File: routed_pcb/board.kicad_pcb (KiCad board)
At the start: 2 copper layers, 100 x 100 mm, 29 parts

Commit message: board cleanup
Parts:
- ?: footprint Button_Switch_SMD:SW_SPST_B3U-1000P -> Library:SW_SPST_B3U-1000P
- B1: footprint kbd:ResetSW -> Library:ResetSW
- MCU1: footprint ProMicro -> Library:ProMicro
- S1, S10, S11, S12, S13, S14, S15, S16, S17, S2, S3, S4, S5, S6, S7, S8, S9: footprint key-switches -> Library:key-switches
- T1: footprint E73:SPDT_C128955 -> Library:SPDT_C128955
- TRRS1: footprint TRRS-PJ-320A-dual -> Library:TRRS-PJ-320A-dual
- _2: footprint JST_PH_S2B-PH-K_02x2.00mm_Angled -> Library:JST_PH_S2B-PH-K_02x2.00mm_Angled
- _3, _4, _5, _6, _7, _8: footprint MountingHole_2.2mm_M2_Pad_Via -> Library:MountingHole_2.2mm_M2_Pad_Via
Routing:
- net VCC: track 210.7 -> 143.3 mm
- net GND: track 180.3 -> 207.1 mm
- net thumb_reachy: track 93.9 -> 81.1 mm
- net matrix_inner_top: track 144.0 -> 154.2 mm, vias 2 -> 3
- net matrix_ring_bottom: track 34.0 -> 40.6 mm
- net Switch18: track 165.7 -> 159.7 mm
- net matrix_index_home: track 70.4 -> 64.9 mm
- net matrix_pinky_bottom: track 40.0 -> 36.2 mm
- net matrix_inner_bottom: track 81.5 -> 78.5 mm
- net matrix_index_bottom: track 62.5 -> 59.5 mm
- net thumb_tucky: track 81.6 -> 79.9 mm
- net matrix_inner_home: track 114.6 -> 113.2 mm
- net RST: track 48.7 -> 47.5 mm

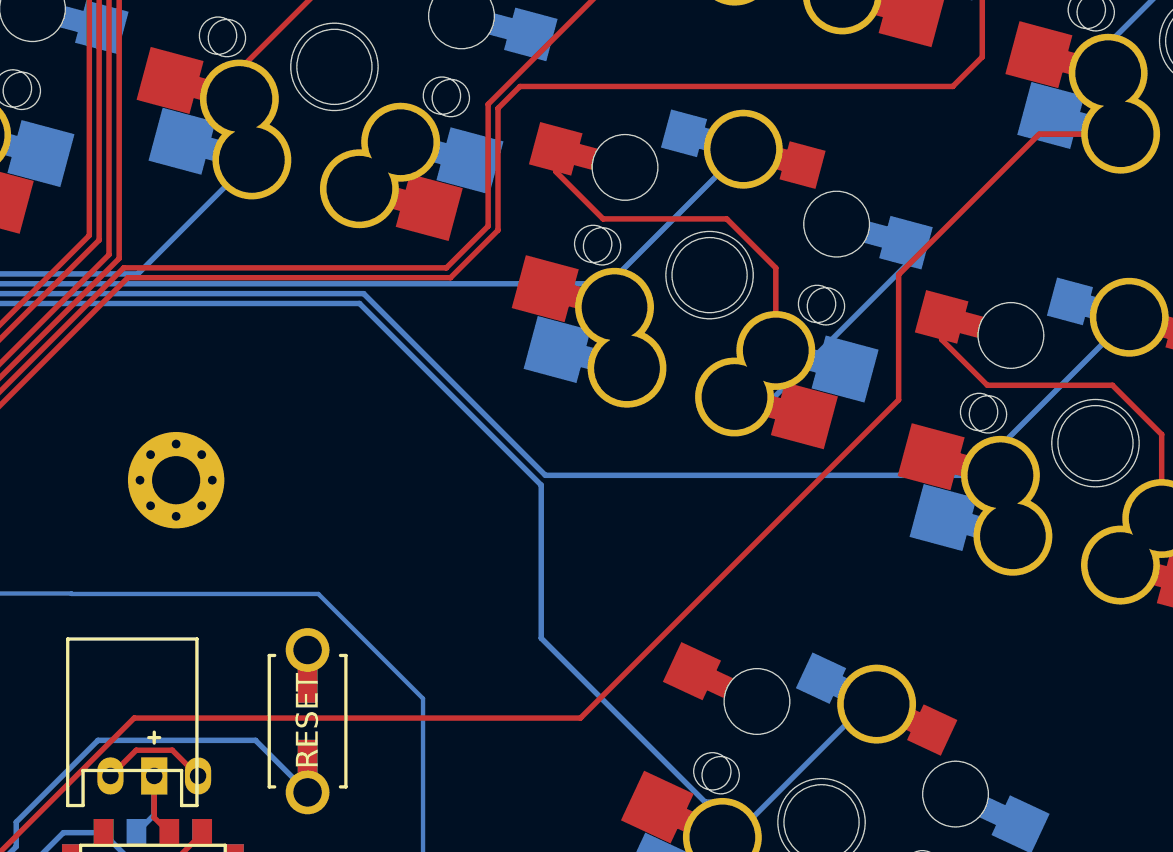
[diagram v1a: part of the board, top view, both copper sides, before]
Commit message: added plate
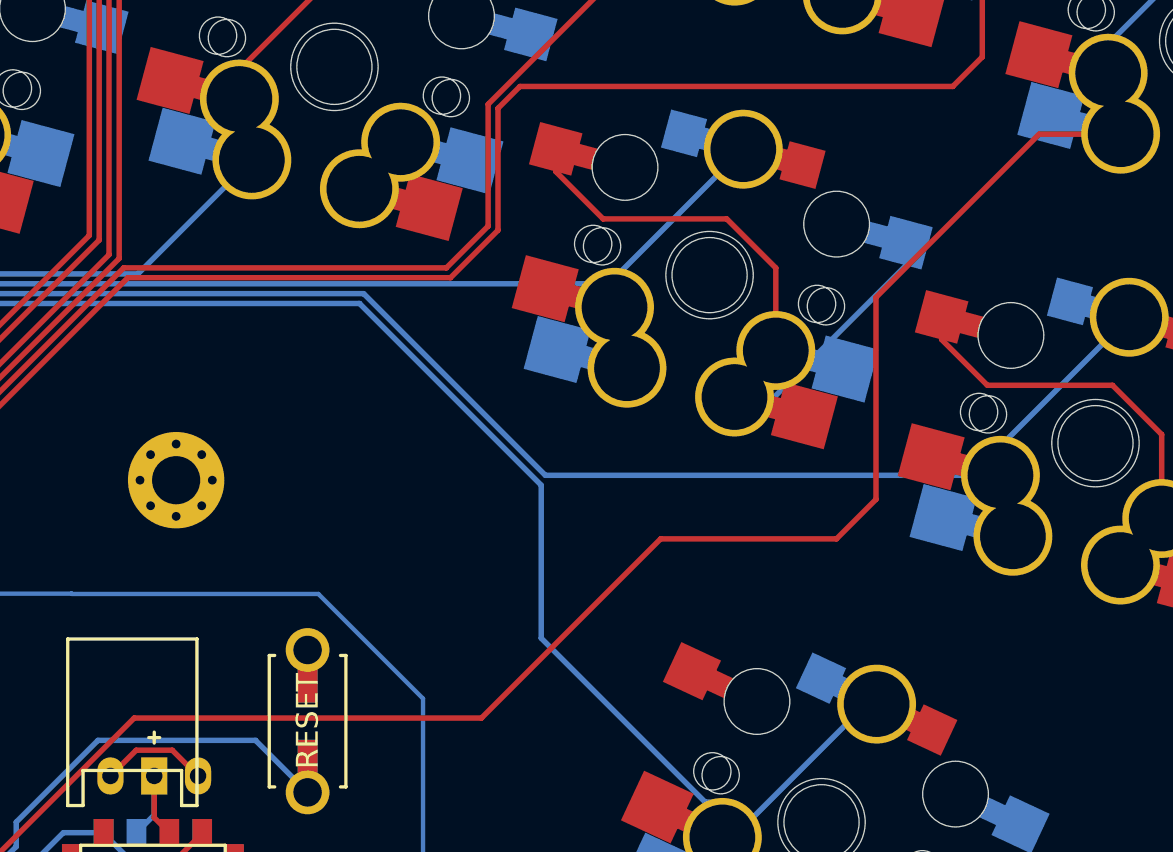
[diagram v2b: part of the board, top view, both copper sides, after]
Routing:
- net matrix_inner_home: track 113.2 -> 115.2 mm
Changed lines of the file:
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@@
       (outputformat 1)
       (mirror false)
-      (drillshape 1)
+      (drillshape 0)
       (scaleselection 1)
-      (outputdirectory "")
+      (outputdirectory "gerbers/")
     )
   )
@@
   (segment (start 146.15277 134.562217) (end 140.275219 140.439768) (width 0.25) (layer "B.Cu") (net 14))
   (segment (start 85.615 139.477518) (end 91.608318 133.4842) (width 0.25) (layer "B.Cu") (net 14))
-  (segment (start 65.005 160.382) (end 65.005 157.951) (width 0.25) (layer "F.Cu") (net 15))
-  (segment (start 135.6288 132.6206) (end 135.6288 138.3356) (width 0.25) (layer "F.Cu") (net 15))
+  (segment (start 65.9312 161.3082) (end 65.005 160.382) (width 0.25) (layer "F.Cu") (net 15))
+  (segment (start 134.5946 133.6548) (end 134.5946 142.875) (width 0.25) (layer "F.Cu") (net 15))
+  (segment (start 116.586 152.8572) (end 100.734652 152.8572) (width 0.25) (layer "F.Cu") (net 15))
   (segment (start 145.762107 126.206388) (end 142.043012 126.206388) (width 0.25) (layer "F.Cu") (net 15))
-  (segment (start 94.0054 160.401) (end 93.0982 161.3082) (width 0.25) (layer "F.Cu") (net 15))
   (segment (start 65.005 157.951) (end 63.88 156.826) (width 0.25) (layer "F.Cu") (net 15))
-  (segment (start 142.043012 126.206388) (end 135.6288 132.6206) (width 0.25) (layer "F.Cu") (net 15))
-  (segment (start 65.9312 161.3082) (end 65.005 160.382) (width 0.25) (layer "F.Cu") (net 15))
-  (segment (start 121.1072 152.8572) (end 100.734652 152.8572) (width 0.25) (layer "F.Cu") (net 15))
+  (segment (start 94.0054 160.401) (end 93.0982 161.3082) (width 0.25) (layer "F.Cu") (net 15))
+  (segment (start 100.734652 152.8572) (end 94.0054 159.586452) (width 0.25) (layer "F.Cu") (net 15))
+  (segment (start 65.005 160.382) (end 65.005 157.951) (width 0.25) (layer "F.Cu") (net 15))
   (segment (start 94.0054 159.586452) (end 94.0054 160.401) (width 0.25) (layer "F.Cu") (net 15))
+  (segment (start 132.7912 144.6784) (end 124.7648 144.6784) (width 0.25) (layer "F.Cu") (net 15))
+  (segment (start 142.043012 126.206388) (end 134.5946 133.6548) (width 0.25) (layer "F.Cu") (net 15))
   (segment (start 93.0982 161.3082) (end 65.9312 161.3082) (width 0.25) (layer "F.Cu") (net 15))
-  (segment (start 135.6288 138.3356) (end 121.1072 152.8572) (width 0.25) (layer "F.Cu") (net 15))
-  (segment (start 100.734652 152.8572) (end 94.0054 159.586452) (width 0.25) (layer "F.Cu") (net 15))
+  (segment (start 134.5946 142.875) (end 132.7912 144.6784) (width 0.25) (layer "F.Cu") (net 15))
+  (segment (start 124.7648 144.6784) (end 116.586 152.8572) (width 0.25) (layer "F.Cu") (net 15))
   (segment (start 151.070332 116.209626) (end 145.192781 122.087177) (width 0.25) (layer "B.Cu") (net 15))
   (segment (start 145.192781 122.087177) (end 145.192781 123.424236) (width 0.25) (layer "B.Cu") (net 15))

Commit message: routed new pcb
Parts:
- removed the ? at (108.7, 153.0)
- removed S1, S10, S11, S12, S13, S14, S15, S16, S17, S2, S3, S4, S5, S6, S7, S8, S9: , Library:key-switches
- removed _2: , Library:JST_PH_S2B-PH-K_02x2.00mm_Angled
- removed _3, _4, _5: , Library:MountingHole_2.2mm_M2_Pad_Via
- added ?: , Button_Switch_SMD:SW_SPST_B3U-1000P, F.Cu at (110.3, 169.0)
- added SW1: , key-switches, F.Cu at (77.0, 118.6)
- added SW10: , key-switches, F.Cu at (133.8, 125.8)
- added SW11: , key-switches, F.Cu at (137.7, 107.2)
- added SW12: , key-switches, F.Cu at (141.7, 88.6)
- added SW13: , key-switches, F.Cu at (151.8, 132.5)
- added SW14: , key-switches, F.Cu at (155.7, 114.0)
- added SW15: , key-switches, F.Cu at (159.7, 95.4)
- added SW16: , key-switches, F.Cu at (118.3, 143.9)
- added SW17: , key-switches, F.Cu at (138.2, 150.7)
- added SW18: , key-switches, F.Cu at (157.8, 160.6)
- added SW2: , key-switches, F.Cu at (81.0, 100.0)
- added SW3: , key-switches, F.Cu at (84.9, 81.4)
- added SW4: , key-switches, F.Cu at (96.6, 117.9)
- added SW5: , key-switches, F.Cu at (100.5, 99.3)
- added SW6: , key-switches, F.Cu at (104.5, 80.7)
- added SW7: , key-switches, F.Cu at (116.2, 117.2)
- added SW8: , key-switches, F.Cu at (120.1, 98.6)
- added SW9: , key-switches, F.Cu at (124.1, 80.0)
- added T2: , E73:SPDT_C128955, F.Cu at (108.3, 161.0)
- added _10: , MountingHole_2.2mm_M2_Pad_Via, F.Cu at (131.3, 168.0)
- added _11: , MountingHole_2.2mm_M2_Pad_Via, F.Cu at (103.3, 135.0)
- added _12: , MountingHole_2.2mm_M2_Pad_Via, F.Cu at (71.3, 168.0)
- added _9: , MountingHole_2.2mm_M2_Pad_Via, F.Cu at (165.3, 140.0)
- B1: footprint Library:ResetSW -> kbd:ResetSW
- MCU1: footprint Library:ProMicro -> ProMicro
- T1: footprint Library:SPDT_C128955 -> E73:SPDT_C128955
- TRRS1: footprint Library:TRRS-PJ-320A-dual -> TRRS-PJ-320A-dual
- _6: footprint Library:MountingHole_2.2mm_M2_Pad_Via -> JST_PH_S2B-PH-K_02x2.00mm_Angled
- _7, _8: footprint Library:MountingHole_2.2mm_M2_Pad_Via -> MountingHole_2.2mm_M2_Pad_Via
- moved _8 107.6 mm to (152.3, 74.0)
- moved _7 74.9 mm to (71.3, 74.0)
- moved _6 26.9 mm to (100.3, 163.0), turned to 180 degrees
- moved B1 16.1 mm to (110.3, 169.0), turned to 180 degrees
- moved T1 9.19 mm to (100.2, 169.2)
- moved TRRS1 8.27 mm to (166.3, 69.3)
- moved MCU1 7.79 mm to (85.5, 153.2), turned to 90 degrees
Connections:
- MCU1 pad 23: Switch18 -> P0
- T1 pad 1: (no net) -> RAW
- T1 pad 3: RAW -> (no net)
- TRRS1 pad 3: Switch18 -> trrs_data
- _6 pad 1: (no net) -> Bplus
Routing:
- net Switch18: track 159.7 -> 0.00 mm
- net trrs_data: track 0.00 -> 140.4 mm, vias 0 -> 1
- net matrix_index_top: track 109.9 -> 174.5 mm, vias 1 -> 2
- net matrix_pinky_bottom: track 36.2 -> 78.0 mm, vias 1 -> 2
- net GND: track 207.1 -> 169.6 mm, vias 0 -> 3
- net RAW: track 45.6 -> 14.2 mm
- net thumb_inner: track 0.00 -> 30.4 mm, vias 0 -> 3
- net matrix_inner_bottom: track 78.5 -> 107.5 mm, vias 0 -> 2
- net P0: track 0.00 -> 25.9 mm, vias 0 -> 1
- net matrix_inner_home: track 115.2 -> 140.7 mm, vias 0 -> 4
- net matrix_ring_bottom: track 40.6 -> 64.2 mm, vias 1 -> 2
- net matrix_middle_home: track 62.2 -> 84.2 mm, vias 0 -> 2
- net VCC: track 143.3 -> 165.2 mm, vias 0 -> 1
- net matrix_ring_top: track 74.5 -> 94.5 mm, vias 1 -> 3
- net thumb_reachy: track 81.1 -> 99.5 mm, vias 0 -> 2
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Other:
- outline, holes or cut-outs redrawn
- board text added: "wired"
- board text added: "wireless"
- board text added: "口"

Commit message: added in schematic
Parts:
- B1, MCU1, SW1, SW10, SW11, SW12, SW13, SW14, SW15, SW16, SW17, SW18, SW2, SW3, SW4, SW5, SW6, SW7, SW8, SW9, T1, T2: value (none) -> ~
- JST1: renamed from _6; value (none) -> ~
- S1: renamed from ?; value (none) -> ~
- renumbered _7 to HOLE1, _8 to HOLE2, _9 to HOLE3, _10 to HOLE4, _11 to HOLE5, _12 to HOLE6
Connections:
- net Bplus renamed /Bplus
- net GND renamed /GND
- net P0 renamed /P0
- net RAW renamed /RAW
- net RST renamed /RST
- net VCC renamed /VCC
- net matrix_index_bottom renamed /matrix_index_bottom
- net matrix_index_home renamed /matrix_index_home
- net matrix_index_top renamed /matrix_index_top
- net matrix_inner_bottom renamed /matrix_inner_bottom
- net matrix_inner_home renamed /matrix_inner_home
- net matrix_inner_top renamed /matrix_inner_top
- net matrix_middle_bottom renamed /matrix_middle_bottom
- net matrix_middle_home renamed /matrix_middle_home
- net matrix_middle_top renamed /matrix_middle_top
- net matrix_pinky_bottom renamed /matrix_pinky_bottom
- net matrix_pinky_home renamed /matrix_pinky_home
- net matrix_pinky_top renamed /matrix_pinky_top
- net matrix_ring_bottom renamed /matrix_ring_bottom
- net matrix_ring_home renamed /matrix_ring_home
- net matrix_ring_top renamed /matrix_ring_top
- net thumb_inner renamed /thumb_inner
- net thumb_reachy renamed /thumb_reachy
- net thumb_tucky renamed /thumb_tucky
- net trrs_data renamed /trrs_data
- T1 pad 3: (no net) -> unconnected-(T1-C-Pad3)
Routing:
- net unconnected-(T1-C-Pad3): vias 0 -> 1

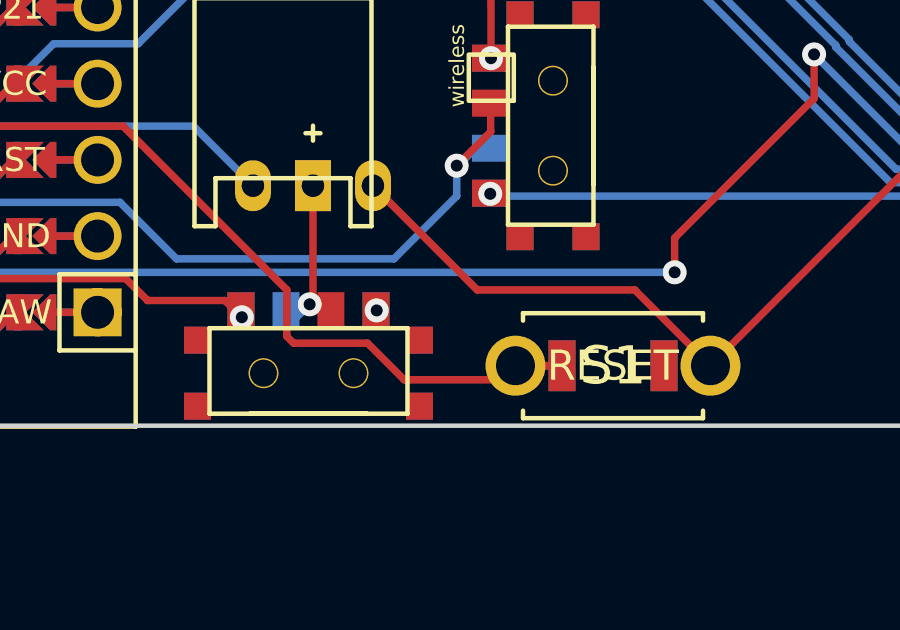
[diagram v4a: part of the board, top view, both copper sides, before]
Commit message: update routed pcb to same as updated config
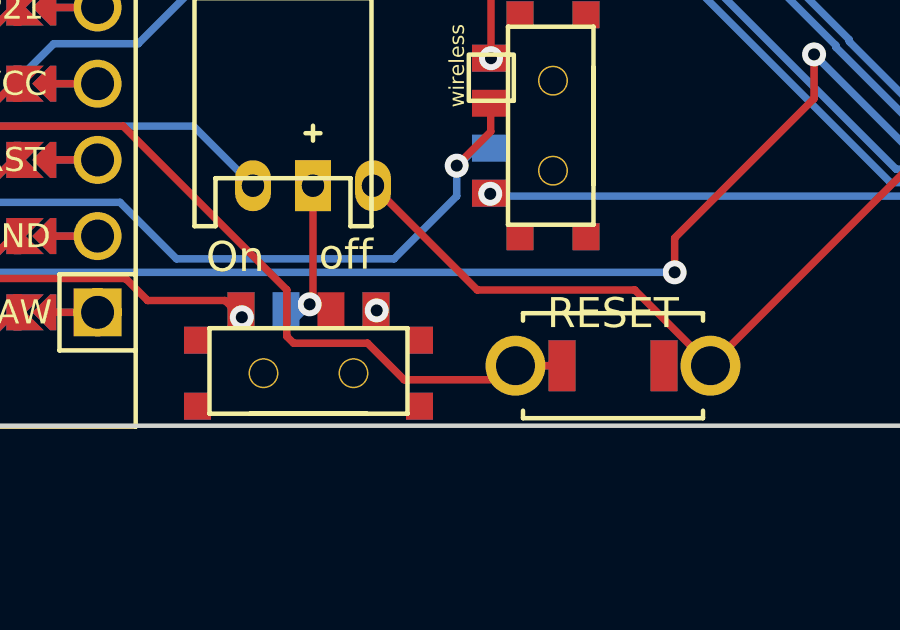
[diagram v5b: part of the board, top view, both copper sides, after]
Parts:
- renumbered S1 to B2
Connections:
- B2 pad 1: /GND -> /RST
- B2 pad 2: /RST -> /GND
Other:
- board text added: "On"
- board text added: "off"
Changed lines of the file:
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@@
       (outputformat 1)
       (mirror false)
-      (drillshape 1)
+      (drillshape 0)
       (scaleselection 1)
-      (outputdirectory "")
+      (outputdirectory "gerbers/")
     )
   )
@@
         (effects (font (size 1 1) (thickness 0.15)))
     )
-    (fp_text user "RESET" (at 0.127 0 180) (layer "B.SilkS")
+    (fp_text user "RESET" (at 0 1.75 180) (layer "B.SilkS")
         (effects (font (size 1 1) (thickness 0.15)) (justify mirror))
     )
-    (fp_text user "RESET" (at 0 0 180) (layer "F.SilkS")
+    (fp_text user "RESET" (at 0 1.75 180) (layer "F.SilkS")
         (effects (font (size 1 1) (thickness 0.15)))
     )
@@
   (footprint "MountingHole_2.2mm_M2_Pad_Via" (layer "F.Cu")
     (at 103.34 135)
+    (attr board_only exclude_from_bom)
     (fp_text reference "HOLE5" (at 0 -3.2) (layer "F.SilkS") hide
         (effects (font (size 1 1) (thickness 0.15)))
@@
   (footprint "MountingHole_2.2mm_M2_Pad_Via" (layer "F.Cu")
     (at 152.34 74)
+    (attr board_only exclude_from_bom)
     (fp_text reference "HOLE2" (at 0 -3.2) (layer "F.SilkS") hide
         (effects (font (size 1 1) (thickness 0.15)))
@@
   (footprint "MountingHole_2.2mm_M2_Pad_Via" (layer "F.Cu")
     (at 71.34 74)
+    (attr board_only exclude_from_bom)
     (fp_text reference "HOLE1" (at 0 -3.2) (layer "F.SilkS") hide
         (effects (font (size 1 1) (thickness 0.15)))
@@
     (property "ki_keywords" "switch normally-open pushbutton push-button")
     (attr smd)
-    (fp_text reference "S1" (at 0 0 180) (layer "F.SilkS")
+    (fp_text reference "B2" (at 0 0 180) (layer "F.SilkS") hide
         (effects (font (size 1.27 1.27) (thickness 0.15)))
     )
-    (fp_text value "~" (at 0 0 180) (layer "F.SilkS")
+    (fp_text value "~" (at 0 0 180) (layer "F.SilkS") hide
         (effects (font (size 1.27 1.27) (thickness 0.15)))
     )
@@
     (fp_circle (center 0 0) (end 0.75 0)
       (stroke (width 0.1) (type solid)) (fill none) (layer "F.Fab"))
-    (pad "1" smd rect (at -1.7 0) (size 0.9 1.7) (layers "F.Cu" "F.Paste" "F.Mask")
-      (net 1 "/GND") (pinfunction "1") (pintype "passive"))
-    (pad "1" smd rect (at -1.7 0) (size 0.9 1.7) (layers "B.Cu" "B.Paste" "B.Mask")
-      (net 1 "/GND") (pinfunction "1") (pintype "passive"))
-    (pad "2" smd rect (at 1.7 0) (size 0.9 1.7) (layers "F.Cu" "F.Paste" "F.Mask")
+    (pad "1" smd rect (at 1.7 0) (size 0.9 1.7) (layers "F.Cu" "F.Paste" "F.Mask")
       (net 2 "/RST") (pinfunction "2") (pintype "passive"))
-    (pad "2" smd rect (at 1.7 0) (size 0.9 1.7) (layers "B.Cu" "B.Paste" "B.Mask")
+    (pad "1" smd rect (at 1.7 0) (size 0.9 1.7) (layers "B.Cu" "B.Paste" "B.Mask")
       (net 2 "/RST") (pinfunction "2") (pintype "passive"))
+    (pad "2" smd rect (at -1.7 0) (size 0.9 1.7) (layers "F.Cu" "F.Paste" "F.Mask")
+      (net 1 "/GND") (pinfunction "1") (pintype "passive"))
+    (pad "2" smd rect (at -1.7 0) (size 0.9 1.7) (layers "B.Cu" "B.Paste" "B.Mask")
+      (net 1 "/GND") (pinfunction "1") (pintype "passive"))
   )
   (footprint "TRRS-PJ-320A-dual" (layer "F.Cu")
@@
   (footprint "MountingHole_2.2mm_M2_Pad_Via" (layer "F.Cu")
     (at 71.34 168)
+    (attr board_only exclude_from_bom)
     (fp_text reference "HOLE6" (at 0 -3.2) (layer "F.SilkS") hide
         (effects (font (size 1 1) (thickness 0.15)))
@@
   (footprint "MountingHole_2.2mm_M2_Pad_Via" (layer "F.Cu")
     (at 165.34 140)
+    (attr board_only exclude_from_bom)
     (fp_text reference "HOLE3" (at 0 -3.2) (layer "F.SilkS") hide
         (effects (font (size 1 1) (thickness 0.15)))
@@
   (footprint "MountingHole_2.2mm_M2_Pad_Via" (layer "F.Cu")
     (at 131.34 168)
+    (attr board_only exclude_from_bom)
     (fp_text reference "HOLE4" (at 0 -3.2) (layer "F.SilkS") hide
         (effects (font (size 1 1) (thickness 0.15)))
@@
     (effects (font (size 1.5 2.2) (thickness 0.15)))
   )
+  (gr_text "off" (at 102.8192 165.8874) (layer "B.SilkS")
+    (effects (font (size 1 1) (thickness 0.15)) (justify left bottom mirror))
+  )
   (gr_text "wired" (at 105.14 163 90) (layer "B.SilkS")
     (effects (font (size 0.5 0.5) (thickness 0.15)))
   )
+  (gr_text "On" (at 98.8314 166.0652) (layer "B.SilkS")
+    (effects (font (size 1 1) (thickness 0.15)) (justify left bottom mirror))
+  )
   (gr_text "口" (at 106.34 159.4 90) (layer "F.SilkS")
     (effects (font (size 1.5 2.2) (thickness 0.15)))
@@
     (effects (font (size 0.5 0.5) (thickness 0.15)))
   )
+  (gr_text "off" (at 100.5332 165.8874) (layer "F.SilkS")
+    (effects (font (size 1 1) (thickness 0.15)) (justify left bottom))
+  )
+  (gr_text "On" (at 96.774 165.9636) (layer "F.SilkS")
+    (effects (font (size 1 1) (thickness 0.15)) (justify left bottom))
+  )
   (segment (start 141.259746 159.184737) (end 141.259746 157.793984) (width 0.25) (layer "F.Cu") (net 1))
